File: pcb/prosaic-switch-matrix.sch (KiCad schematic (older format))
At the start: 142 parts, among them K1 ESC, K10 WIN, K11 2, K12 W, K13 S, K14 X, K15 LALT, K16 3, K17 E, K18 D, K19 C, K2 TAB, K20 SPACE, K21 4, K22 R, K23 F, K24 V, K25 RALT, K26 5, K27 T, K28 G, K29 B, K3 CAPSLK, K30 FN, K31 6, K32 Y, K33 H, K34 N, K35 MENU, K36 7, K37 U, K38 J, K39 M, K4 LSHIFT, K40 RCTRL, K41 8, K42 I, K43 K, K44 ,, K45 LEFT, K46 9, K47 O, K48 L, K49 ., K5 LCTRL, K50 DOWN, K51 0, K52 P, K53 ;, K54 /, K55 RIGHT, K56 -, K57 [, K58 ', K59 RSHIFT, K6 1, K60 =, K61 ], K62 ENTER, K63 UP, K64 BCKSPC, K65 \\, K66 HOME, K67 END, K68 INS, K69 DEL, K7 Q, K70 PGUP, K71 PGDWN, K8 A, K9 Z

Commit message: Made moutning hole rearrangements
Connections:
- net col10: now also K30.1; no longer K55.1
- net col11: now also K35.1
- net col12: now also K40.1; no longer K63.1
- net col13: no longer K66.1, K67.1
- net col14: now also K45.1; no longer K70.1, K71.1
- net col3: no longer K20.1
- net col4: no longer K25.1
- net col5: now also K20.1; no longer K30.1
- net col6: no longer K35.1
- net col7: no longer K40.1
- net col8: no longer K45.1
- net col9: now also K25.1; no longer K50.1
- net row0: now also D66.1 (K), D70.1 (K)
- net row1: now also D67.1 (K), D71.1 (K)
- net row2: no longer D66.1 (K), D70.1 (K)
- net row3: no longer D67.1 (K), D71.1 (K)
- new net col15: K50.1, K63.1, K66.1, K67.1
- new net col16: K55.1, K70.1, K71.1
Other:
- moved on the sheet: D1, D10, D11, D12, D13, D14, D15, D16, D17, D18, D19, D2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

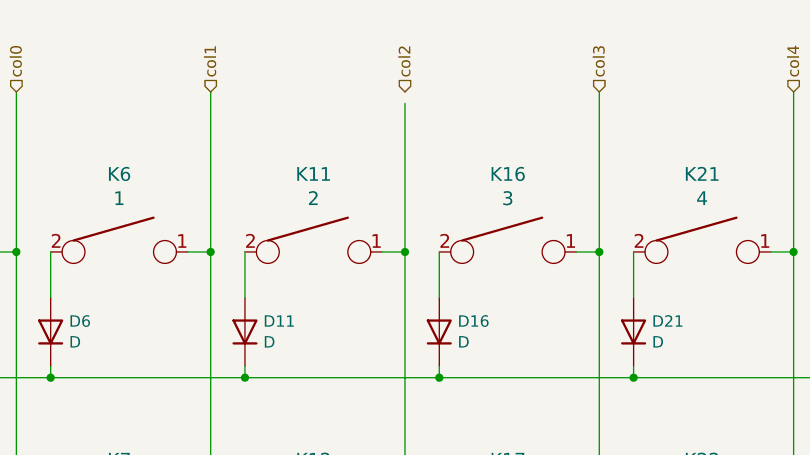
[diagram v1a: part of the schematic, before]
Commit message: WIP: Ready for stabilizer verification
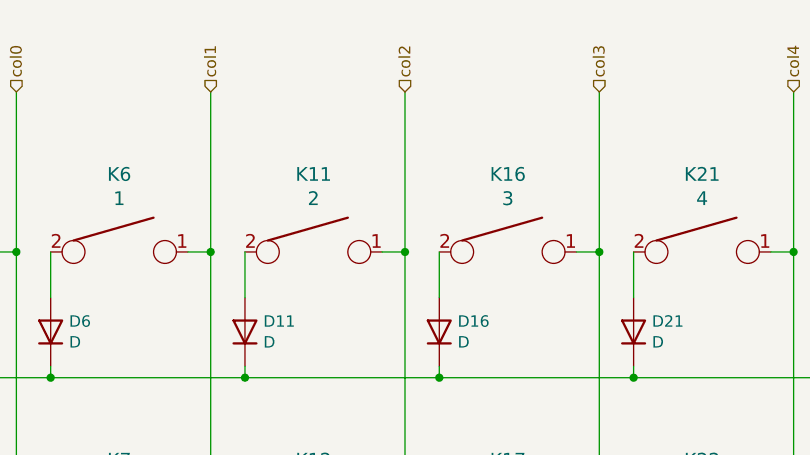
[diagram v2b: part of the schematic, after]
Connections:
- net col2: now also K11.1, K12.1, K13.1, K14.1, K15.1
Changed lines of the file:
@@
 Connection ~ 3050 6200
-Wire Wire Line
-	3900 1800 3900 2450
 Wire Wire Line
 	3900 2450 3800 2450
@@
 	5750 8000 9150 8000
 Connection ~ 5750 8000
+Wire Wire Line
+	3900 1750 3900 2450
 $EndSCHEMATC

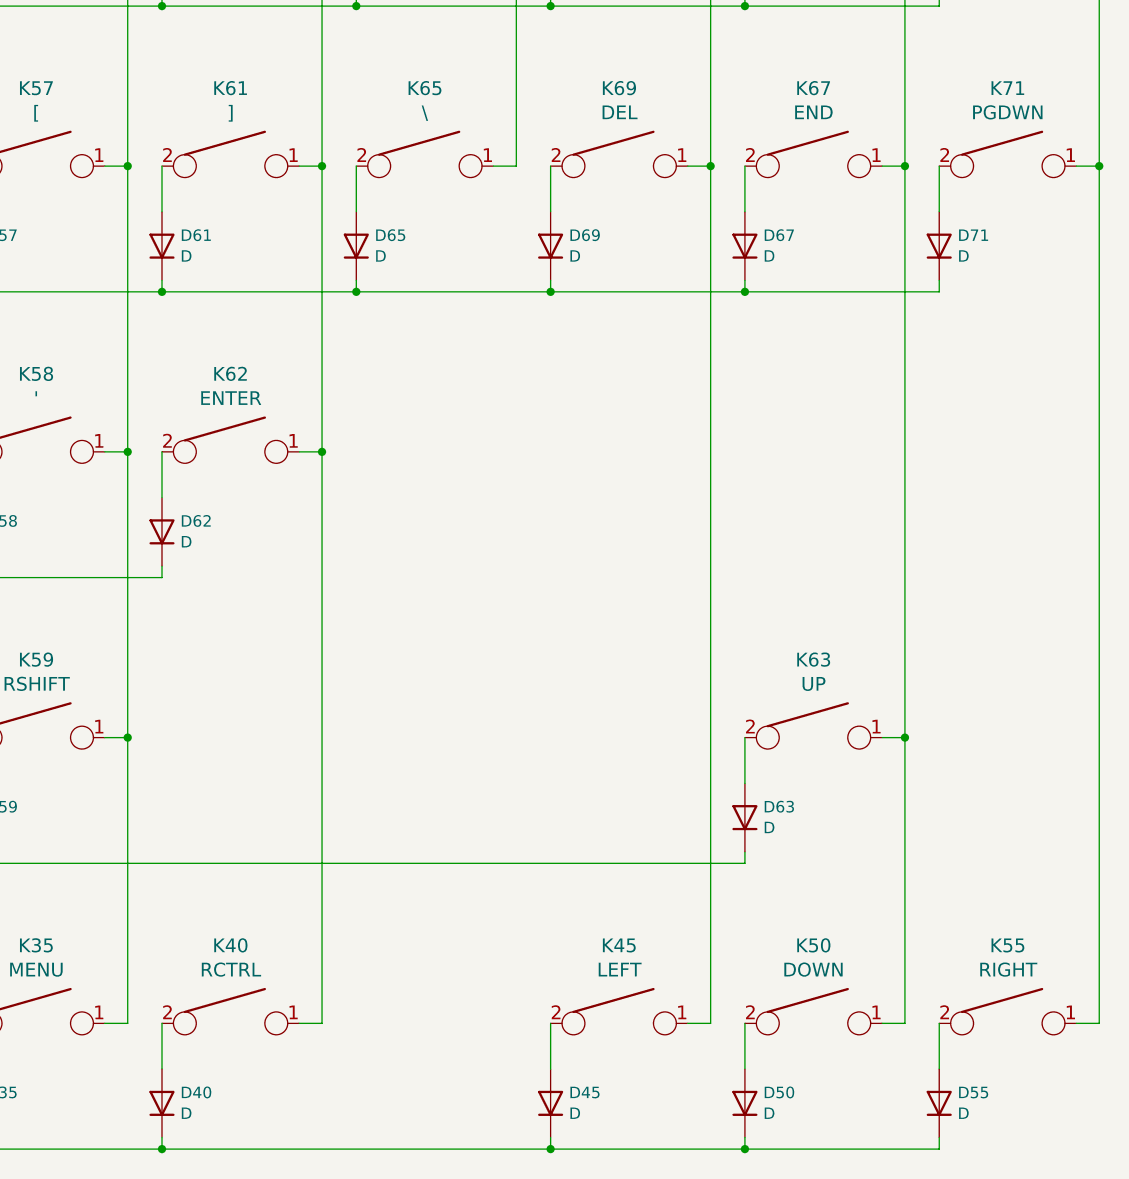
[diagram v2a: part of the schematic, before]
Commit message: Completed revision with new PCB layout
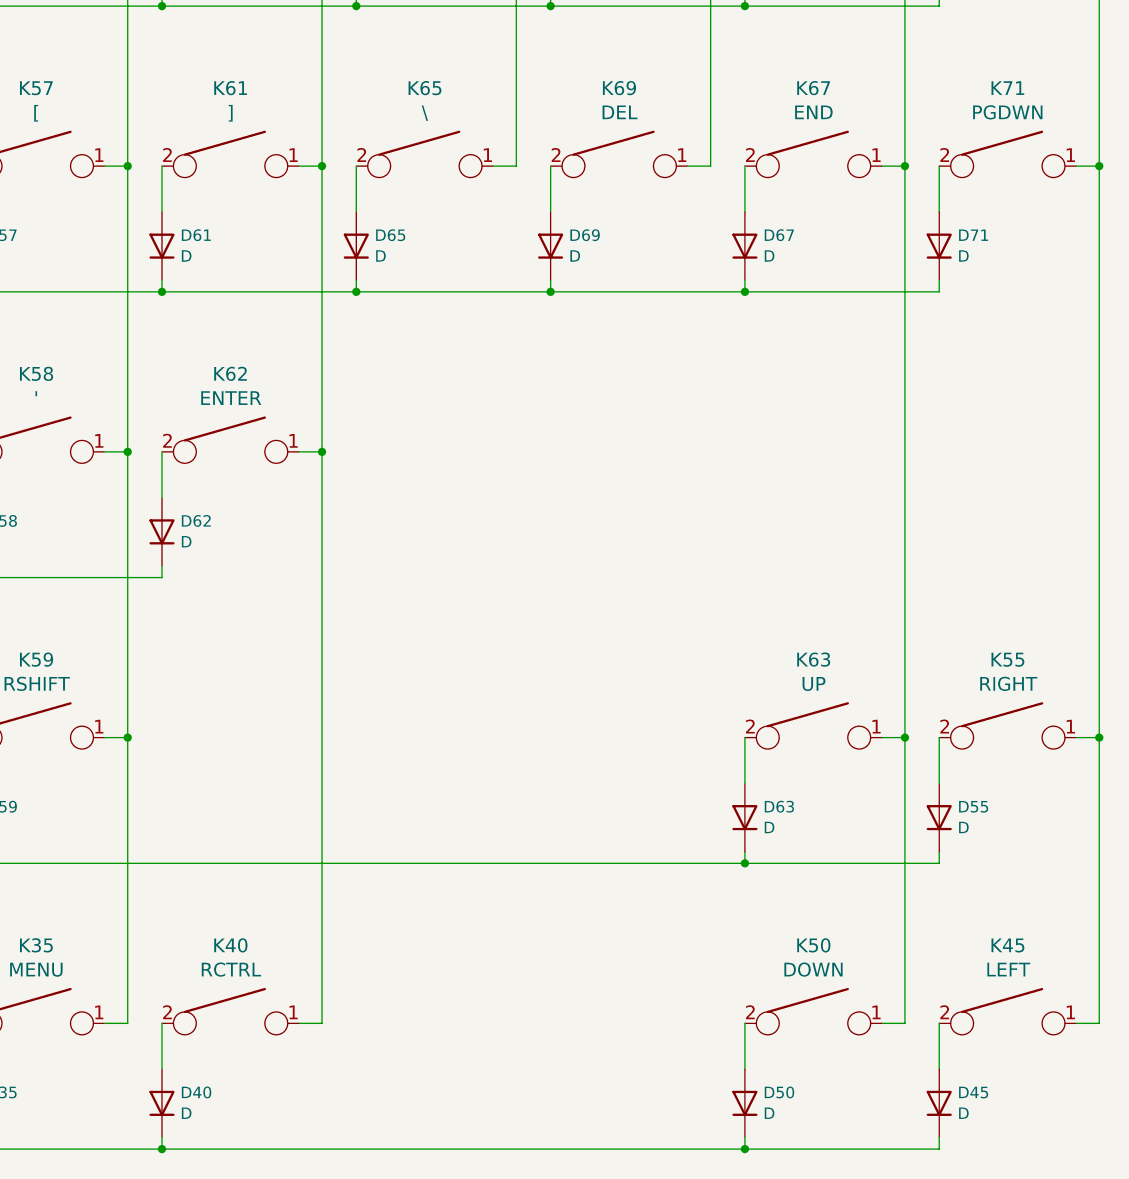
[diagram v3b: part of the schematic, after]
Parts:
- K20: footprint keebs:Mx_Alps_625 -> keebs:Mx_Alps_625_reverse
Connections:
- net col14: no longer K45.1
- net col16: now also K45.1
- net row3: now also D55.1 (K)
- net row4: no longer D55.1 (K)
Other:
- moved on the sheet: D45, D55, K45, K55
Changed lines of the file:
@@
 F 0 "K20" H 6050 7789 60  0000 C CNN
 F 1 "SPACE" H 6050 7683 60  0000 C CNN
-F 2 "keebs:Mx_Alps_625" H 6050 7450 60  0001 C CNN
+F 2 "keebs:Mx_Alps_625_reverse" H 6050 7450 60  0001 C CNN
 F 3 "" H 6050 7450 60  0000 C CNN
 	1    6050 7450
@@
 L keyboard_parts:KEYSW K45
 U 1 1 5F2B3486
-P 13700 7450
-F 0 "K45" H 13700 7789 60  0000 C CNN
-F 1 "LEFT" H 13700 7683 60  0000 C CNN
-F 2 "keebs:Mx_Alps_100" H 13700 7450 60  0001 C CNN
-F 3 "" H 13700 7450 60  0000 C CNN
-	1    13700 7450
+P 15400 7450
+F 0 "K45" H 15400 7789 60  0000 C CNN
+F 1 "LEFT" H 15400 7683 60  0000 C CNN
+F 2 "keebs:Mx_Alps_100" H 15400 7450 60  0001 C CNN
+F 3 "" H 15400 7450 60  0000 C CNN
+	1    15400 7450
 	1    0    0    -1
 $EndComp
@@
 L Device:D D45
 U 1 1 5F2B348C
-P 13400 7800
-F 0 "D45" V 13446 7720 50  0000 R CNN
-F 1 "D" V 13355 7720 50  0000 R CNN
-F 2 "keyboard_parts:D_SOD123_axial" H 13400 7800 50  0001 C CNN
-F 3 "~" H 13400 7800 50  0001 C CNN
-	1    13400 7800
+P 15100 7800
+F 0 "D45" V 15146 7720 50  0000 R CNN
+F 1 "D" V 15055 7720 50  0000 R CNN
+F 2 "keyboard_parts:D_SOD123_axial" H 15100 7800 50  0001 C CNN
+F 3 "~" H 15100 7800 50  0001 C CNN
+	1    15100 7800
 	0    -1   -1   0
 $EndComp
@@
 L keyboard_parts:KEYSW K55
 U 1 1 5F2B349E
-P 15400 7450
-F 0 "K55" H 15400 7789 60  0000 C CNN
-F 1 "RIGHT" H 15400 7683 60  0000 C CNN
-F 2 "keebs:Mx_Alps_100" H 15400 7450 60  0001 C CNN
-F 3 "" H 15400 7450 60  0000 C CNN
-	1    15400 7450
+P 15400 6200
+F 0 "K55" H 15400 6539 60  0000 C CNN
+F 1 "RIGHT" H 15400 6433 60  0000 C CNN
+F 2 "keebs:Mx_Alps_100" H 15400 6200 60  0001 C CNN
+F 3 "" H 15400 6200 60  0000 C CNN
+	1    15400 6200
 	1    0    0    -1
 $EndComp
@@
 L Device:D D55
 U 1 1 5F2B34A4
-P 15100 7800
-F 0 "D55" V 15146 7720 50  0000 R CNN
-F 1 "D" V 15055 7720 50  0000 R CNN
-F 2 "keyboard_parts:D_SOD123_axial" H 15100 7800 50  0001 C CNN
-F 3 "~" H 15100 7800 50  0001 C CNN
-	1    15100 7800
+P 15100 6550
+F 0 "D55" V 15146 6470 50  0000 R CNN
+F 1 "D" V 15055 6470 50  0000 R CNN
+F 2 "keyboard_parts:D_SOD123_axial" H 15100 6550 50  0001 C CNN
+F 3 "~" H 15100 6550 50  0001 C CNN
+	1    15100 6550
 	0    -1   -1   0
 $EndComp
@@
 Connection ~ 10850 8000
 Wire Wire Line
-	13400 7450 13400 7650
-Wire Wire Line
-	13400 7950 13400 8000
+	15100 7450 15100 7650
 Wire Wire Line
 	14250 7450 14250 7650
@@
 	14250 7950 14250 8000
 Wire Wire Line
-	14250 8000 13400 8000
-Connection ~ 13400 8000
-Wire Wire Line
-	15100 7450 15100 7650
-Wire Wire Line
-	15100 7950 15100 8000
-Wire Wire Line
-	15100 8000 14250 8000
-Connection ~ 14250 8000
+	15100 6200 15100 6400
+Wire Wire Line
+	15100 6700 15100 6750
 Text HLabel 1000 3000 0    50   Input ~ 0
 row0
@@
 Connection ~ 9000 4950
 Wire Wire Line
-	14100 7450 14000 7450
+	15800 7450 15700 7450
 Wire Wire Line
 	9850 1750 9850 2450
@@
 Connection ~ 10700 4950
 Wire Wire Line
-	15800 7450 15700 7450
+	15800 6200 15700 6200
 Wire Wire Line
 	11550 1750 11550 2450
@@
 Connection ~ 15800 2450
 Connection ~ 14950 6200
-Wire Wire Line
-	14100 3700 14100 7450
-Connection ~ 14100 3700
-Wire Wire Line
-	14950 3700 14950 6200
-Connection ~ 14950 3700
-Wire Wire Line
-	15800 3700 15800 7450
 Connection ~ 15800 3700
-Wire Wire Line
-	10850 6750 14250 6750
-Connection ~ 10850 6750
-Wire Wire Line
-	11700 8000 13400 8000
-Connection ~ 11700 8000
 Connection ~ 9850 6200
 Connection ~ 10700 6200
@@
 Wire Wire Line
 	3900 1750 3900 2450
+Wire Wire Line
+	15800 6200 15800 7450
+Wire Wire Line
+	15100 8000 15100 7950
+Connection ~ 11700 8000
+Wire Wire Line
+	10850 6750 14250 6750
+Connection ~ 10850 6750
+Connection ~ 14950 3700
+Wire Wire Line
+	14950 3700 14950 6200
+Wire Wire Line
+	15800 3700 15800 6200
+Wire Wire Line
+	14250 6750 15100 6750
+Connection ~ 14250 6750
+Connection ~ 14250 8000
+Wire Wire Line
+	14250 8000 15100 8000
+Connection ~ 15800 6200
+Wire Wire Line
+	11700 8000 14250 8000
 $EndSCHEMATC
